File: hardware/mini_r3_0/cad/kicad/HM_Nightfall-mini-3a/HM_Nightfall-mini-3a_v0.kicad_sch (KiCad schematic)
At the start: 97 parts, among them J2 FAN_2S3S, K1 62201021121, P1 JST-PH2, Q2 SI7135DP-T1-GE3, Q3 PMPB13XNE,115, U1 AP2210N-3.3TRG1, U2 MP6551GQB-P, U3 MP6551GQB-P, U4 ISM330DHCXTR, U5 STM32F413CHU6TRUFQFPN-48_7X7X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, U6 CY15B108QI-20LPXC, U7 MPM3610GQV-P

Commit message: Improve mini 3S schematic readability
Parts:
- removed C22: 10u/25V X7R, HM_Nightfall-mini-2e_v1:C0805, symbol HM_Nightfall-mini-2e_v1-eagle-import:C-EUC0402
- removed C23: 22u/10V X7R, HM_Nightfall-mini-2e_v1:C0805, symbol HM_Nightfall-mini-2e_v1-eagle-import:C-EUC0402
- removed C24: 0.1u/25V X7R, HM_Nightfall-mini-2e_v1:C0402, symbol HM_Nightfall-mini-2e_v1-eagle-import:C-EUC0402
- removed D4: BAS16WT1GW, HM_Nightfall-mini-2e_v1:SOT323, symbol HM_Nightfall-mini-2e_v1-eagle-import:BAS16WT1GW
- removed POWER0: EG1215AA, HM_Nightfall-mini-2e_v1:SW_EG1215AA, symbol HM_Nightfall-mini-2e_v1-eagle-import:EG1215AA
- removed R12, R32: 10k, HM_Nightfall-mini-2e_v1:R0402, symbol HM_Nightfall-mini-2e_v1-eagle-import:R-EU_R0402
- removed R29, R31, R4: 100k, HM_Nightfall-mini-2e_v1:R0402, symbol HM_Nightfall-mini-2e_v1-eagle-import:R-EU_R0402
- removed R30: 19.1k, HM_Nightfall-mini-2e_v1:R0402, symbol HM_Nightfall-mini-2e_v1-eagle-import:R-EU_R0402
- removed R5: 27k, HM_Nightfall-mini-2e_v1:R0402, symbol HM_Nightfall-mini-2e_v1-eagle-import:R-EU_R0402
- added C22: 10u/25V X7R, HM_Nightfall-mini-2e_v1:C0805, symbol Nightfall-Power:C_VERTICAL
- added C23: 22u/10V X7R, HM_Nightfall-mini-2e_v1:C0805, symbol Nightfall-Power:C_VERTICAL
- added C24: 0.1u/25V X7R, HM_Nightfall-mini-2e_v1:C0402, symbol Nightfall-Power:C_VERTICAL
- added D4: BAS16WT1GW, HM_Nightfall-mini-2e_v1:SOT323, symbol Nightfall-Power:D_VERTICAL
- added POWER0: EG1215AA, HM_Nightfall-mini-2e_v1:SW_EG1215AA, symbol Nightfall-Power:SW_SPDT_VERTICAL
- added R12, R29, R31, R4: 100k, HM_Nightfall-mini-2e_v1:R0402, symbol Nightfall-Power:R_VERTICAL
- added R30: 19.1k, HM_Nightfall-mini-2e_v1:R0402, symbol Nightfall-Power:R_VERTICAL
- added R32: 10k, HM_Nightfall-mini-2e_v1:R0402, symbol Nightfall-Power:R_VERTICAL
- added R5: 27k, HM_Nightfall-mini-2e_v1:R0402, symbol Nightfall-Power:R_VERTICAL
- P1: value JST-PH2 -> BATTERY; footprint HM_Nightfall-mini-2e_v1:JST-PH2 -> HM_Nightfall-mini-2e_v1:JST_PH2
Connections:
- net +5V: now also C23.1, R29.2
- net FAN_PWM: now also R32.1
- net GND2: now also C22.2, C23.2, POWER0.1 (OFF), R30.2, R32.2, R5.1
- net VBAT_SW: now also C22.1, C24.1, D4.3 (K), R31.2, R4.2
- net VOL_CHECK: now also R4.1, R5.2
- net FAN_NEG renamed FAN_NEG_INTERNAL
- net FAN_NEG_INTERNAL: now also C24.2, D4.1 (A)
- net MPM_EN renamed MPM_EN_INTERNAL
- net MPM_EN_INTERNAL: now also R31.1
- net MPM_FB renamed MPM_FB_INTERNAL
- net MPM_FB_INTERNAL: now also R29.1, R30.1
- net PWR_GATE renamed PWR_GATE_INTERNAL
- net PWR_GATE_INTERNAL: now also POWER0.2 (COM), R12.1
- net VBAT_RAW: no longer names the net of P1.2, Q2.1 (S), Q2.2 (S), Q2.3 (S)
- net VBAT_RAW: now also R12.2
- no-connect marks 8 -> 5
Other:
- note added: "2S-3S BATTERY / MAIN SWITCH"
- note added: "2S-3S POWER: VBAT_SW -> MPM3610 -> +5V"
- note added: "SUCTION FAN / 2S-3S"
- note removed: "2S-3S POWER: VBAT_SW -> MPM3610 -> +5V (logic only)"
- note removed: "D4 flyback; C24 motor-noise suppression"
- note removed: "FB: 100k / 19.1k = 4.98V typ"
- note removed: "SUCTION FAN (2S-3S rated)"
- note removed: "VBAT ADC: 100k / 27k; 12.6V -> 2.68V"

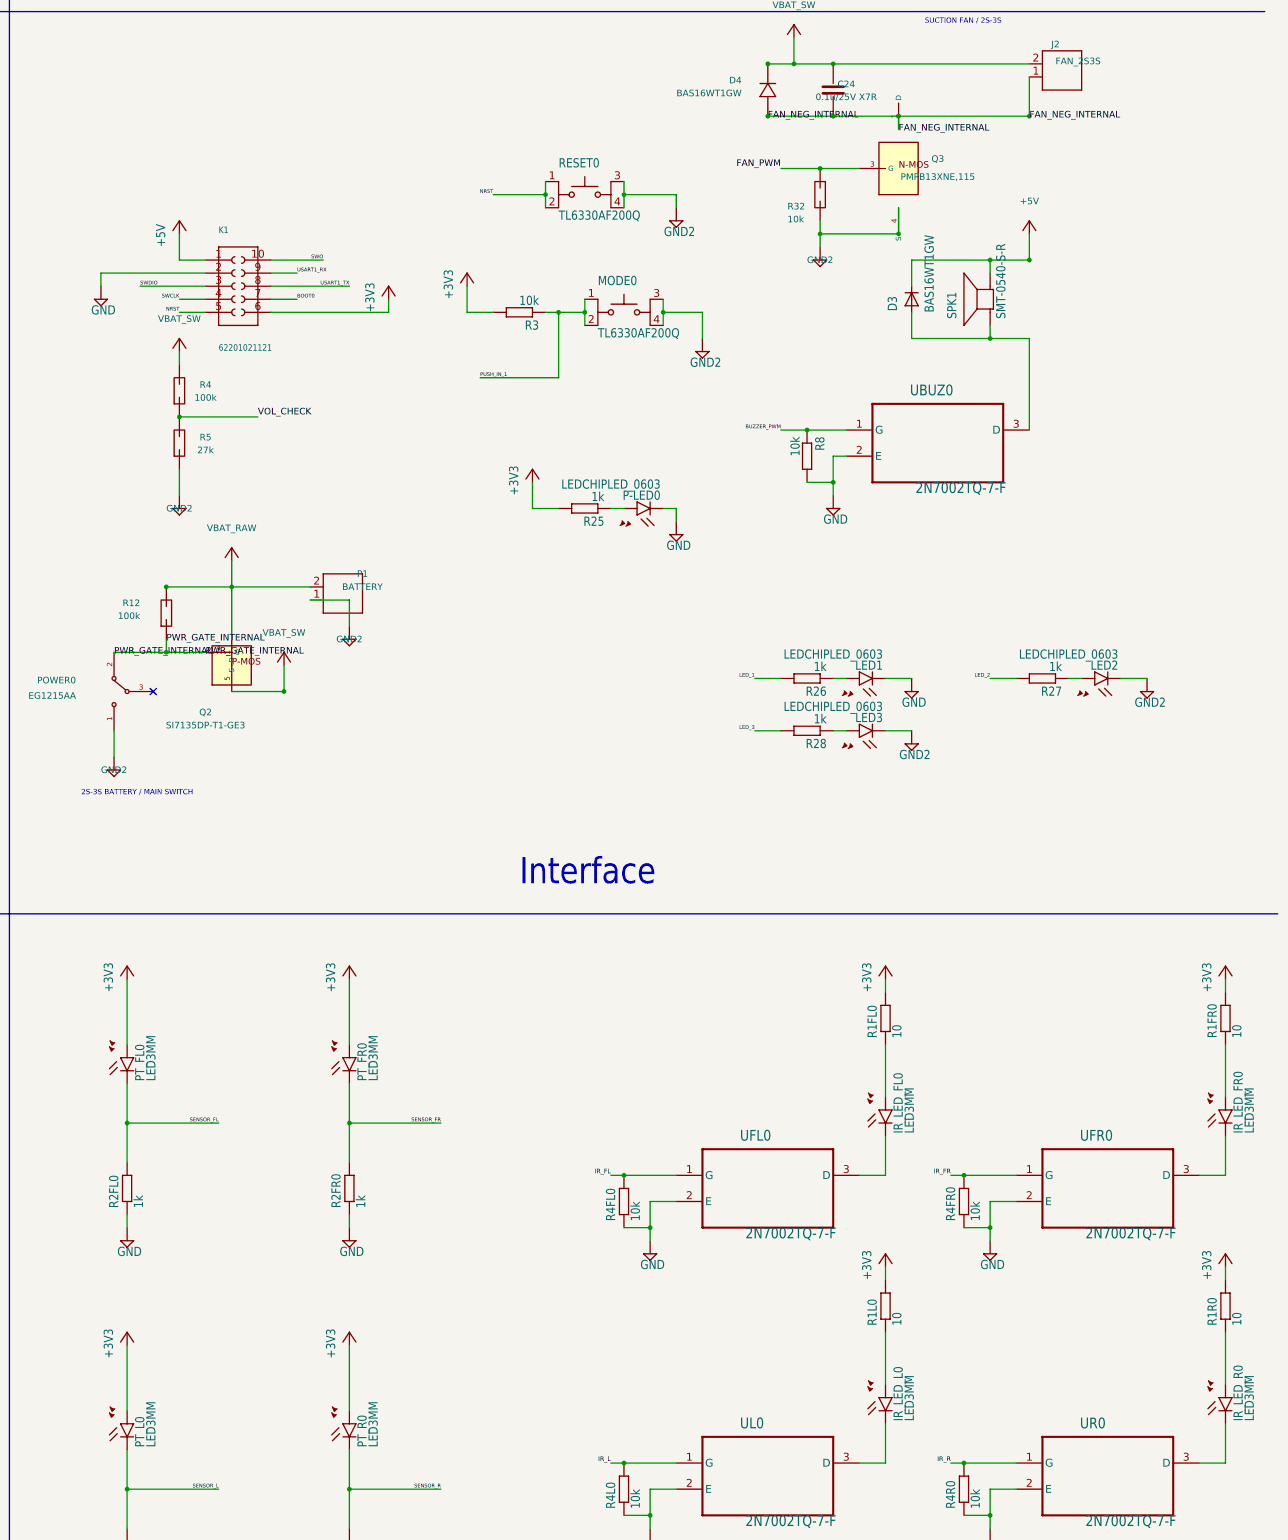
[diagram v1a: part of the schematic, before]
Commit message: Use SOT-23 MOSFET for suction fan
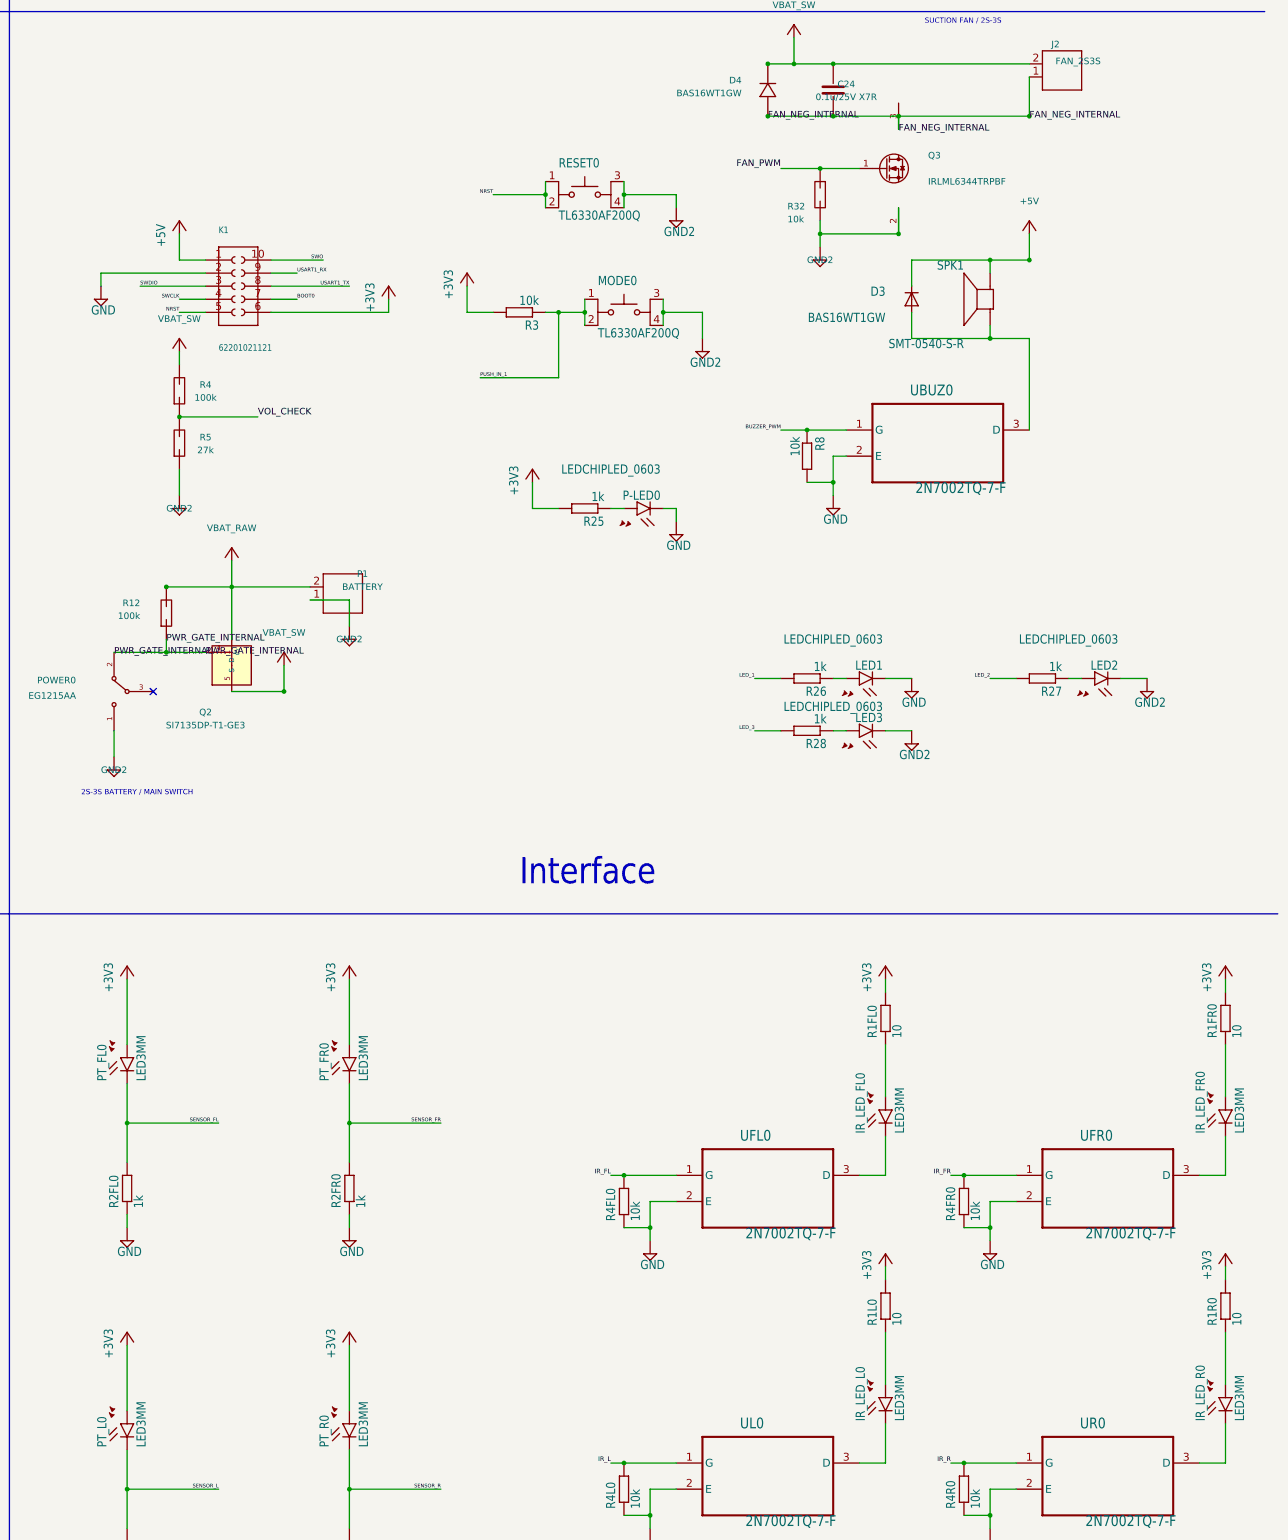
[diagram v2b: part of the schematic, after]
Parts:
- Q3: value PMPB13XNE,115 -> IRLML6344TRPBF; footprint Nightfall-Power:DFN2020MD-6_SOT1220 -> Package_TO_SOT_SMD:SOT-23; symbol Nightfall-Power:PMPB13XNE,115 -> Nightfall-Power:IRLML6344TRPBF
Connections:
- net FAN_NEG_INTERNAL: now also Q3.3 (D); no longer Q3.1 (D), Q3.2 (D), Q3.5 (D), Q3.6 (D), Q3.7 (D)
- net FAN_PWM: now also Q3.1 (G); no longer Q3.3 (G)
- net GND2: now also Q3.2 (S); no longer Q3.4 (S), Q3.8 (S)
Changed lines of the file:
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@@
 		(dnp no)
 		(property "Reference" "IR_LED_R0"
-			(at 465.836 362.712 90)
+			(at 458.470 362.712 90)
 			(show_name no)
 			(do_not_autoplace no)
@@
 		)
 		(property "Value" "LED3MM"
-			(at 467.995 362.712 90)
+			(at 466.090 362.712 90)
 			(show_name no)
 			(do_not_autoplace no)
@@
 		)
 		(property "Value" "LEDCHIPLED_0603"
-			(at 352.552 179.705 90)
+			(at 352.552 176.784 90)
 			(show_name no)
 			(do_not_autoplace no)
@@
 		(dnp no)
 		(property "Reference" "PT_R0"
-			(at 295.656 367.792 90)
+			(at 288.290 367.792 90)
 			(show_name no)
 			(do_not_autoplace no)
@@
 		)
 		(property "Value" "LED3MM"
-			(at 297.815 367.792 90)
+			(at 295.910 367.792 90)
 			(show_name no)
 			(do_not_autoplace no)
@@
 		)
 		(property "Value" "LEDCHIPLED_0603"
-			(at 441.452 212.725 90)
+			(at 441.452 209.804 90)
 			(show_name no)
 			(do_not_autoplace no)
@@
 		(dnp no)
 		(property "Reference" "PT_FR0"
-			(at 295.656 296.672 90)
+			(at 288.290 296.672 90)
 			(show_name no)
 			(do_not_autoplace no)
@@
 		)
 		(property "Value" "LED3MM"
-			(at 297.815 296.672 90)
+			(at 295.910 296.672 90)
 			(show_name no)
 			(do_not_autoplace no)
@@
 		(dnp no)
 		(property "Reference" "IR_LED_FL0"
-			(at 399.796 306.832 90)
+			(at 392.430 306.832 90)
 			(show_name no)
 			(do_not_autoplace no)
@@
 		)
 		(property "Value" "LED3MM"
-			(at 401.955 306.832 90)
+			(at 400.050 306.832 90)
 			(show_name no)
 			(do_not_autoplace no)
@@
 		(dnp no)
 		(property "Reference" "SPK1"
-			(at 410.21 148.59 0)
+			(at 411.48 137.16 90)
 			(show_name no)
 			(do_not_autoplace no)
@@
 		)
 		(property "Value" "SMT-0540-S-R"
-			(at 419.735 148.59 0)
+			(at 411.48 152.40 90)
 			(show_name no)
 			(do_not_autoplace no)
@@
 		(dnp no)
 		(property "Reference" "PT_FL0"
-			(at 252.476 296.672 90)
+			(at 245.110 296.672 90)
 			(show_name no)
 			(do_not_autoplace no)
@@
 		)
 		(property "Value" "LED3MM"
-			(at 254.635 296.672 90)
+			(at 252.730 296.672 90)
 			(show_name no)
 			(do_not_autoplace no)
@@
 		(dnp no)
 		(property "Reference" "PT_L0"
-			(at 252.476 367.792 90)
+			(at 245.110 367.792 90)
 			(show_name no)
 			(do_not_autoplace no)
@@
 		)
 		(property "Value" "LED3MM"
-			(at 254.635 367.792 90)
+			(at 252.730 367.792 90)
 			(show_name no)
 			(do_not_autoplace no)
@@
 		(dnp no)
 		(property "Reference" "IR_LED_L0"
-			(at 399.796 362.712 90)
+			(at 392.430 362.712 90)
 			(show_name no)
 			(do_not_autoplace no)
@@
 		)
 		(property "Value" "LED3MM"
-			(at 401.955 362.712 90)
+			(at 400.050 362.712 90)
 			(show_name no)
 			(do_not_autoplace no)
@@
 		)
 		(property "Value" "LEDCHIPLED_0603"
-			(at 395.732 212.725 90)
+			(at 395.732 209.804 90)
 			(show_name no)
 			(do_not_autoplace no)
@@
 		(dnp no)
 		(property "Reference" "IR_LED_FR0"
-			(at 465.836 306.832 90)
+			(at 458.470 306.832 90)
 			(show_name no)
 			(do_not_autoplace no)
@@
 		)
 		(property "Value" "LED3MM"
-			(at 467.995 306.832 90)
+			(at 466.090 306.832 90)
 			(show_name no)
 			(do_not_autoplace no)
@@
 		(dnp no)
 		(property "Reference" "D3"
-			(at 398.6731 147.0959 0)
+			(at 396.24 142.24 90)
 			(show_name no)
 			(do_not_autoplace no)
@@
 		)
 		(property "Value" "BAS16WT1GW"
-			(at 405.8184 147.3468 0)
+			(at 396.24 147.32 90)
 			(show_name no)
 			(do_not_autoplace no)
@@
 	)
 	(symbol
-		(lib_id "Nightfall-Power:PMPB13XNE,115")
+		(lib_id "Nightfall-Power:IRLML6344TRPBF")
 		(at 398.78 119.38 0)
 		(unit 1)
@@
 		(dnp no)
 		(property "Reference" "Q3"
-			(at 406.4 117.5 0)
+			(at 404.495 116.84 0)
 			(show_name no)
 			(do_not_autoplace no)
 			(effects
 				(font (size 1.27 1.27))
+				(justify left)
 			)
 		)
-		(property "Value" "PMPB13XNE,115"
-			(at 406.4 121 0)
+		(property "Value" "IRLML6344TRPBF"
+			(at 404.495 121.92 0)
 			(show_name no)
 			(do_not_autoplace no)
 			(effects
 				(font (size 1.27 1.27))
+				(justify left)
 			)
 		)
-		(property "Footprint" "Nightfall-Power:DFN2020MD-6_SOT1220"
+		(property "Footprint" "Package_TO_SOT_SMD:SOT-23"
 			(at 398.78 119.38 0)
 			(hide yes)
 			(show_name no)
 			(do_not_autoplace no)
-			(effects
-				(font (size 1.27 1.27))
-			)
+			(effects (font (size 1.27 1.27)))
 		)
-		(property "Datasheet" "https://assets.nexperia.com/documents/data-sheet/PMPB13XNE.pdf"
+		(property "Datasheet" "https://www.infineon.com/assets/row/public/documents/24/49/infineon-irlml6344-datasheet-en.pdf"
 			(at 398.78 119.38 0)
 			(hide yes)
 			(show_name no)
 			(do_not_autoplace no)
-			(effects
-				(font (size 1.27 1.27))
-			)
+			(effects (font (size 1.27 1.27)))
 		)
-		(property "Description" ""
+		(property "Description" "30 V logic-level N-channel MOSFET, SOT-23; fan low-side PWM switch. G=1, S=2, D=3."
 			(at 398.78 119.38 0)
 			(hide yes)
 			(show_name no)
 			(do_not_autoplace no)
-			(effects
-				(font (size 1.27 1.27))
-			)
+			(effects (font (size 1.27 1.27)))
 		)
 		(pin "1")
 		(pin "2")
 		(pin "3")
-		(pin "4")
-		(pin "5")
-		(pin "6")
-		(pin "7")
-		(pin "8")
 		(instances
 			(project "HM_Nightfall-mini-3a_v0"

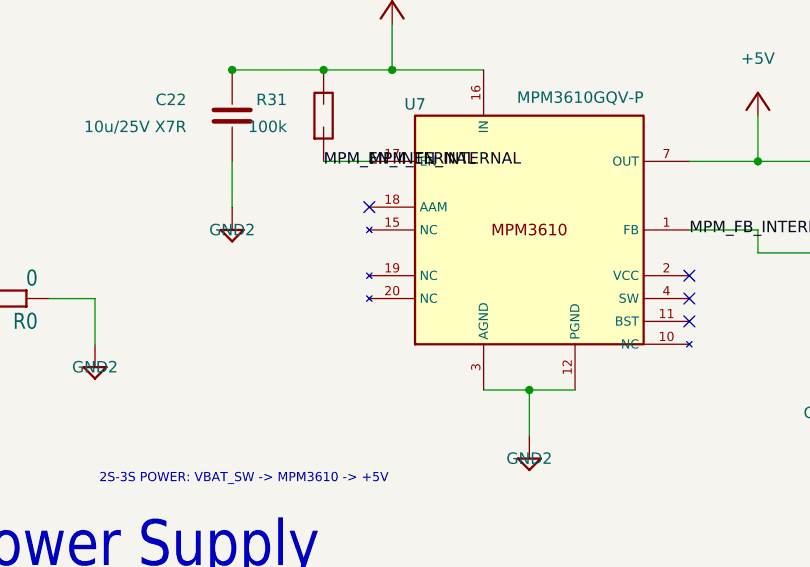
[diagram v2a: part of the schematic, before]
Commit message: Place mini_r3 PCB components from DXF
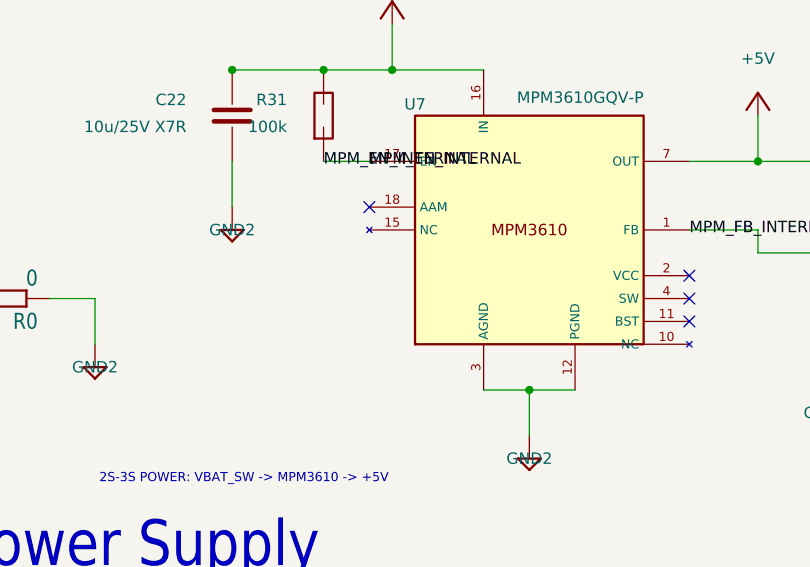
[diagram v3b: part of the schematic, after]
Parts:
- C22, C23: footprint HM_Nightfall-mini-2e_v1:C0805 -> Capacitor_SMD:C_0805_2012Metric
- C24: footprint HM_Nightfall-mini-2e_v1:C0402 -> Capacitor_SMD:C_0402_1005Metric
- D4: footprint HM_Nightfall-mini-2e_v1:SOT323 -> Package_TO_SOT_SMD:SOT-323_SC-70
- J2: footprint HM_Nightfall-mini-2e_v1:JST_PH2 -> Connector_JST:JST_PH_B2B-PH-K_1x02_P2.00mm_Vertical
- Q2: footprint Package_SO:PowerPAK_SO-8_Single -> Nightfall-Power:PowerPAK_SO-8_FullPins
- R29, R30, R31, R32: footprint HM_Nightfall-mini-2e_v1:R0402 -> Resistor_SMD:R_0402_1005Metric
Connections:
- net VBAT_RAW: now reaches P1.2, Q2.1 (S), Q2.2 (S), Q2.3 (S), R12.2
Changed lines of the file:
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@@
 			)
 		)
-		(property "Footprint" "HM_Nightfall-mini-2e_v1:C0805"
+		(property "Footprint" "Capacitor_SMD:C_0805_2012Metric"
 			(at 365.76 33.02 0)
 			(hide yes)
@@
 			)
 		)
-		(property "Footprint" "HM_Nightfall-mini-2e_v1:R0402"
+		(property "Footprint" "Resistor_SMD:R_0402_1005Metric"
 			(at 375.92 33.02 0)
 			(hide yes)
@@
 			)
 		)
-		(property "Footprint" "HM_Nightfall-mini-2e_v1:R0402"
+		(property "Footprint" "Resistor_SMD:R_0402_1005Metric"
 			(at 431.8 43.18 0)
 			(hide yes)
@@
 			)
 		)
-		(property "Footprint" "HM_Nightfall-mini-2e_v1:R0402"
+		(property "Footprint" "Resistor_SMD:R_0402_1005Metric"
 			(at 431.8 53.34 0)
 			(hide yes)
@@
 			)
 		)
-		(property "Footprint" "HM_Nightfall-mini-2e_v1:C0805"
+		(property "Footprint" "Capacitor_SMD:C_0805_2012Metric"
 			(at 449.58 43.18 0)
 			(hide yes)
@@
 			)
 		)
-		(property "Footprint" "HM_Nightfall-mini-2e_v1:R0402"
+		(property "Footprint" "Resistor_SMD:R_0402_1005Metric"
 			(at 383.54 124.46 0)
 			(hide yes)
@@
 			)
 		)
-		(property "Footprint" "HM_Nightfall-mini-2e_v1:JST_PH2"
+		(property "Footprint" "Connector_JST:JST_PH_B2B-PH-K_1x02_P2.00mm_Vertical"
 			(at 431.8 101.6 0)
 			(hide yes)
@@
 			)
 		)
-		(property "Footprint" "HM_Nightfall-mini-2e_v1:SOT323"
+		(property "Footprint" "Package_TO_SOT_SMD:SOT-323_SC-70"
 			(at 373.38 104.14 0)
 			(hide yes)
@@
 			)
 		)
-		(property "Footprint" "HM_Nightfall-mini-2e_v1:C0402"
+		(property "Footprint" "Capacitor_SMD:C_0402_1005Metric"
 			(at 386.08 104.14 0)
 			(hide yes)
@@
 			)
 		)
-		(property "Footprint" "Package_SO:PowerPAK_SO-8_Single"
+		(property "Footprint" "Nightfall-Power:PowerPAK_SO-8_FullPins"
 			(at 269.24 215.9 0)
 			(hide yes)
